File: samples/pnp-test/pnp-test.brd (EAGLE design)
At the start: 76 x 76 mm, 38 parts

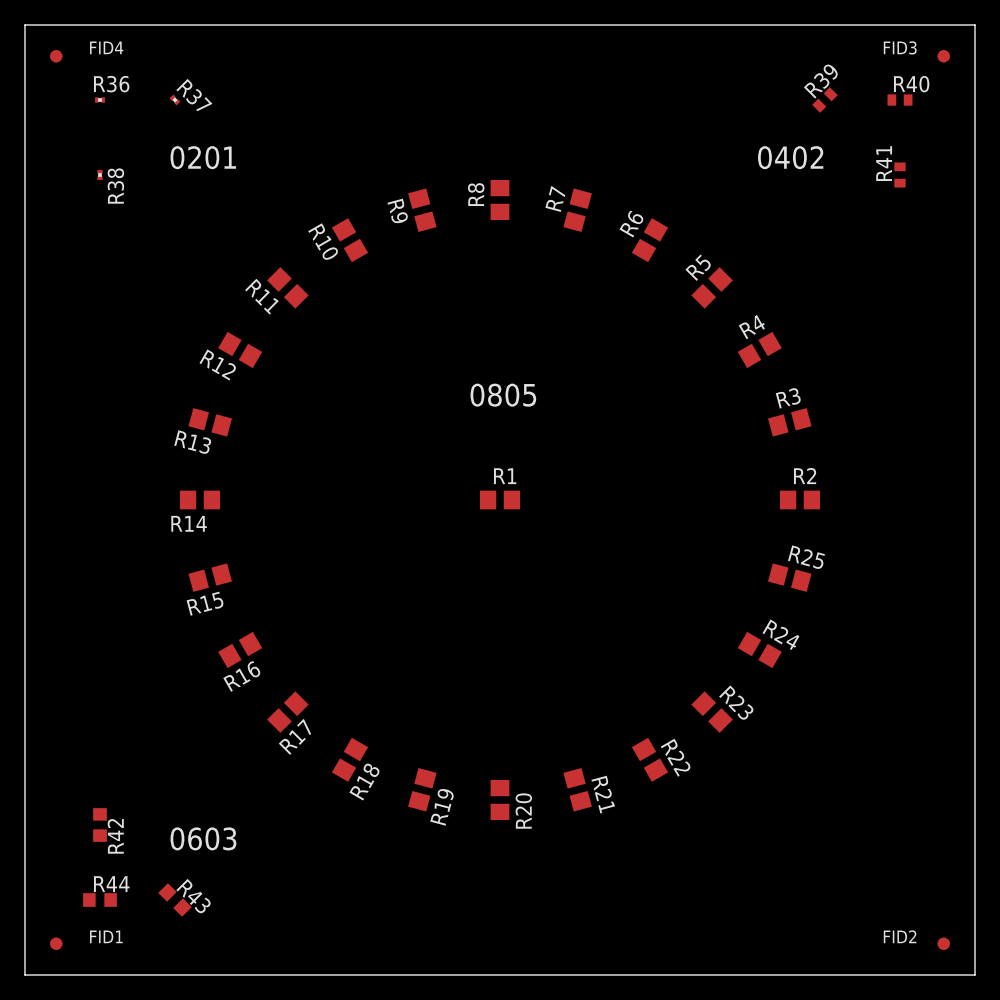
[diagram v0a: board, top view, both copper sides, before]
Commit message: Updated the pnp-test board to have components on the back side to improve testability. Created a new pnp-test.png used for the default ImageCamera that includes two top and two bottom versions of the board. Removed a bunch of cruft that is no longer needed now that we have the Eagle importer.
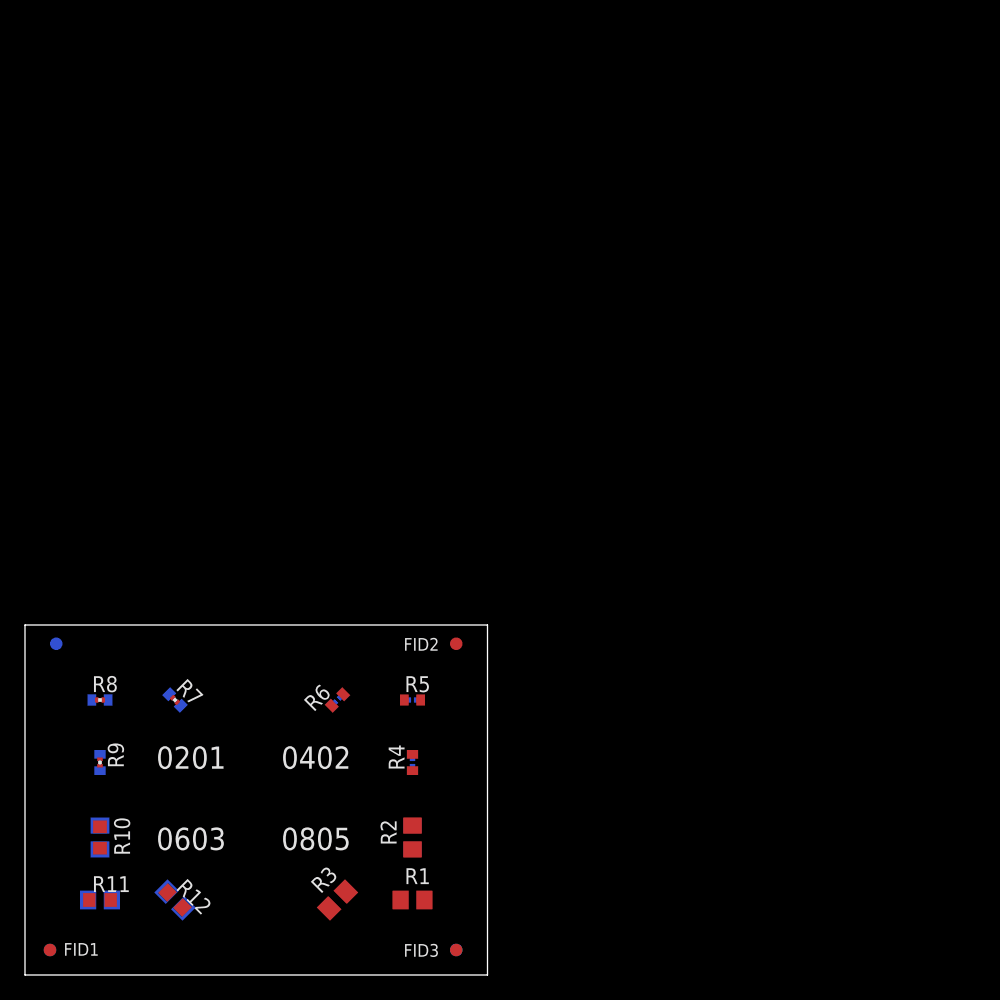
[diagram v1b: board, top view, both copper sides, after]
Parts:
- removed R25: 1K, rcl:R0805
- removed R36, R37, R38: 1K, rcl:R0201
- removed R39, R40, R41: 1K, rcl:R0402
- removed R42, R43, R44: 1K, rcl:R0603
- added FID5, FID6: FIDUCIAL1X2, SparkFun:FIDUCIAL-1X2
- R10, R11, R12, R20, R21, R22: device rcl:R0805 -> rcl:R0603
- R14, R15, R16, R7, R8, R9: device rcl:R0805 -> rcl:R0201
- R17, R18, R19, R4, R5, R6: device rcl:R0805 -> rcl:R0402
- moved FID3 81.4 mm to (34.5, 2.00)
- moved FID4 78.3 mm to (34.5, 2.00), flipped to the bottom
- moved R3 52.6 mm to (25.0, 6.00), turned to 45 degrees
- moved R10 51.8 mm to (6.00, 11.0), turned to 270 degrees
- moved R8 51.2 mm to (6.00, 22.0), turned to 0 degrees
- moved R11 51.2 mm to (6.00, 6.00), turned to 0 degrees
- moved R9 51.2 mm to (6.00, 17.0), turned to 270 degrees
- moved R24 50.9 mm to (12.0, 6.00), flipped to the bottom, turned to 45 degrees
- moved R7 50.7 mm to (12.0, 22.0), turned to 315 degrees
- moved R23 50.0 mm to (6.00, 11.0), flipped to the bottom, turned to 90 degrees
- moved FID2 45.8 mm to (34.5, 26.5)
- moved R6 44.5 mm to (25.0, 22.0), turned to 45 degrees
- moved R12 44.3 mm to (12.0, 6.00), turned to 315 degrees
- moved R4 43.1 mm to (31.0, 17.0), turned to 90 degrees
- moved R2 41.1 mm to (31.0, 11.0), turned to 90 degrees
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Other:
- board size 76 x 76 mm -> 37 x 28 mm
- board text added: "FID5"
- board text added: "FID6"
